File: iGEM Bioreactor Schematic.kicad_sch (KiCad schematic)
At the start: 13 parts, among them M1 Motor_AC, M2 Motor_Servo, Q1 Q_Photo_NPN, U1 OLED_display_1, U2 Pico, U3 L293D, U4 DS18B20, U5 L298N

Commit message: for datalogger
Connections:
- net at U2.1 (GPIO0/I2C0_SDA): now also U2.8 (GND)
- no-connect marks 44 -> 42
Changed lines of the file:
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@@
   (junction (at 172.72 74.93) (diameter 0) (color 0 0 0 0)
   )
-  (no_connect (at 93.98 44.45))
   (no_connect (at 124.46 171.45))
   (no_connect (at 121.92 171.45))
@@
   (no_connect (at 93.98 67.31))
   (no_connect (at 93.98 52.07))
-  (no_connect (at 93.98 62.23))
   (no_connect (at 93.98 64.77))
   (no_connect (at 144.78 82.55))
@@
     (stroke (width 0) (type default) (color 0 0 0 0))
   )
+  (wire (pts (xy 91.44 62.23) (xy 93.98 62.23))
+    (stroke (width 0) (type default) (color 0 0 0 0))
+  )
+  (wire (pts (xy 93.98 44.45) (xy 91.44 44.45))
+    (stroke (width 0) (type default) (color 0 0 0 0))
+  )
   (wire (pts (xy 147.32 46.99) (xy 151.13 46.99))
     (stroke (width 0) (type default) (color 0 0 0 0))
@@
     (stroke (width 0) (type default) (color 0 0 0 0))
   )
+  (wire (pts (xy 91.44 44.45) (xy 91.44 62.23))
+    (stroke (width 0) (type default) (color 0 0 0 0))
+  )

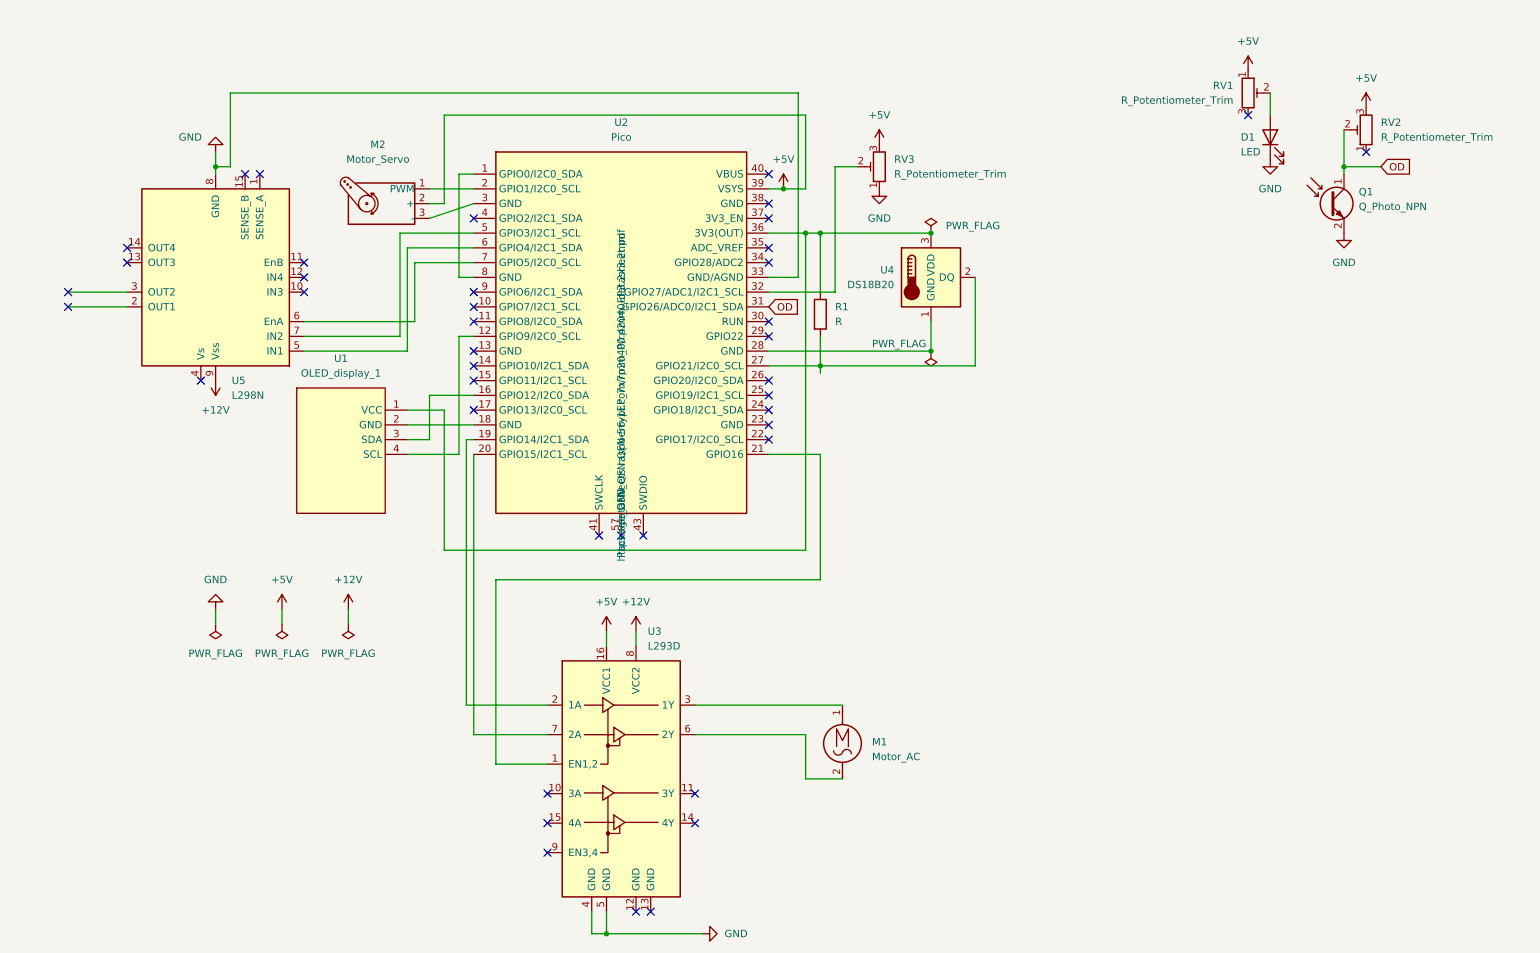
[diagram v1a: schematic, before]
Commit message: Clean up schematic
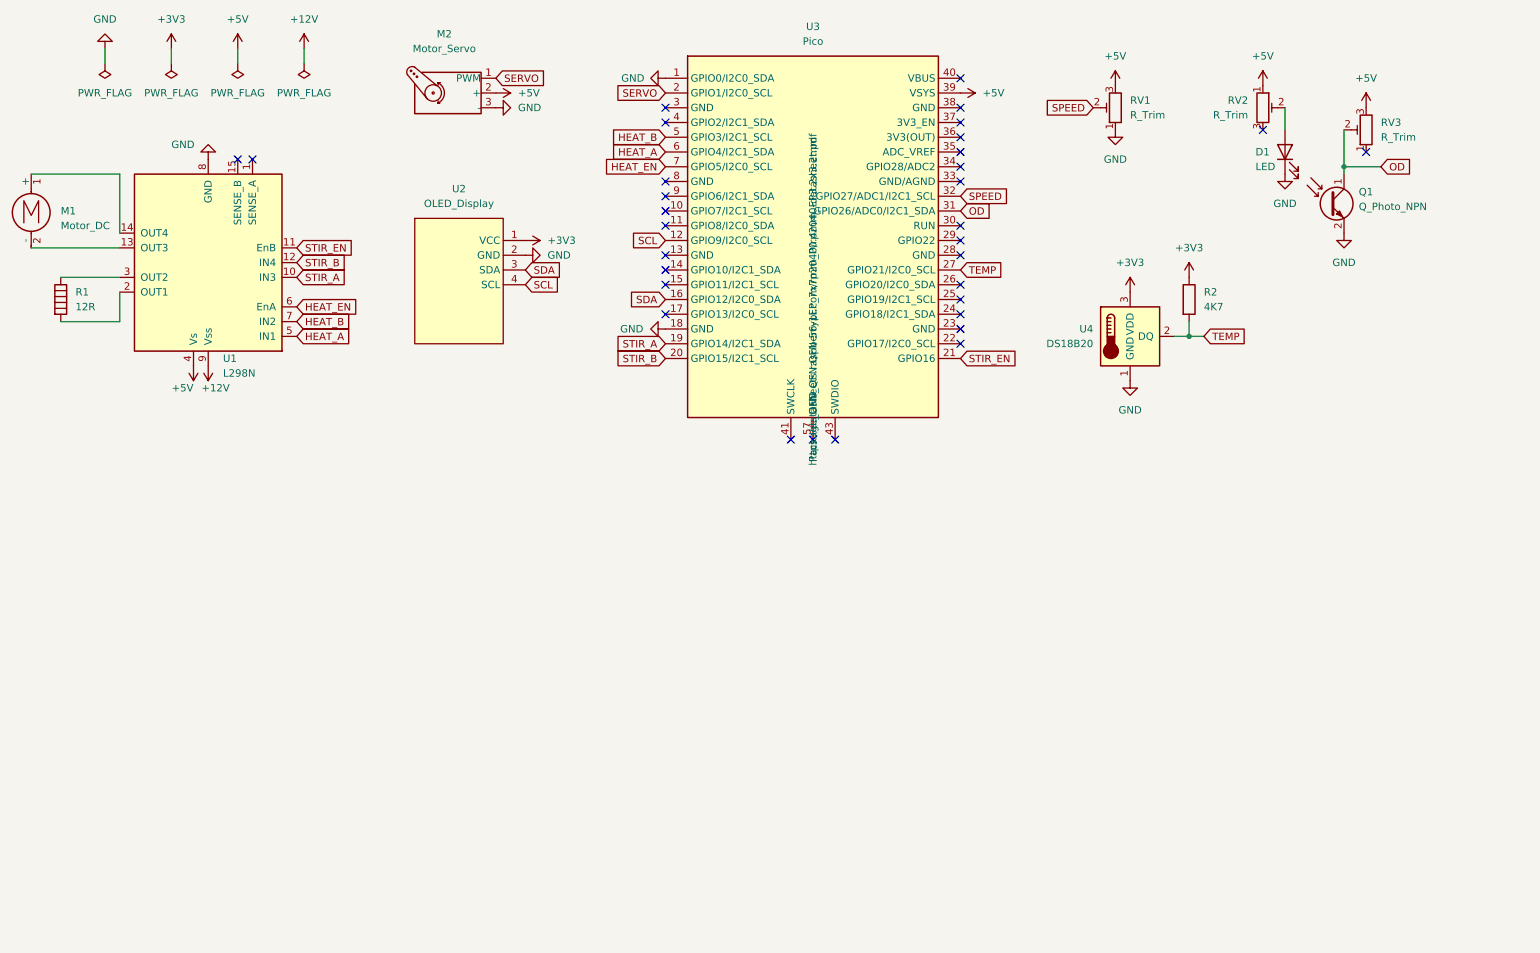
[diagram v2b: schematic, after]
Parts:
- removed M1: Motor_AC, symbol Motor:Motor_AC
- removed U3: L293D, Package_DIP:DIP-16_W7.62mm, symbol Driver_Motor:L293D
- added M1: Motor_DC, symbol Motor:Motor_DC
- added R1: 12R, symbol Device:Heater
- R2: renamed from R1; value R -> 4K7
- RV1: renamed from RV3; value R_Potentiometer_Trim -> R_Trim
- RV2: renamed from RV1; value R_Potentiometer_Trim -> R_Trim
- RV3: renamed from RV2; value R_Potentiometer_Trim -> R_Trim
- U2: renamed from U1; value OLED_display_1 -> OLED_Display
- renumbered U5 to U1, U2 to U3
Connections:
- net +5V: now also U1.4 (Vs)
- net GND: now also M2.3 (-), U2.2 (GND), U3.1 (GPIO0/I2C0_SDA), U3.18 (GND), U4.1 (GND); no longer U3.33 (GND/AGND)
- net STIR_EN: now reaches U3.21 (GPIO16)
- net STIR_EN: now also U1.11 (EnB)
- net STIR_A: now reaches U3.19 (GPIO14/I2C1_SDA)
- net STIR_A: now also U1.10 (IN3)
- net STIR_B: now reaches U3.20 (GPIO15/I2C1_SCL)
- net STIR_B: now also U1.12 (IN4)
- net SERVO: now reaches M2.1 (PWM), U3.2 (GPIO1/I2C0_SCL)
- net at U3.3 (GND): no longer M2.3 (-)
- net +3V3: now reaches R2.1, U2.1 (VCC), U4.3 (VDD)
- net +3V3: no longer U3.36 (3V3(OUT))
- net SDA: now reaches U2.3 (SDA), U3.16 (GPIO12/I2C0_SDA)
- net SCL: now reaches U2.4 (SCL), U3.12 (GPIO9/I2C0_SCL)
- net TEMP: now reaches R2.2, U3.27 (GPIO21/I2C0_SCL), U4.2 (DQ)
- net at U3.8 (GND): no longer U3.1 (GPIO0/I2C0_SDA)
- net at U3.28 (GND): no longer U4.1 (GND)
- net SPEED: now reaches RV1.2, U3.32 (GPIO27/ADC1/I2C1_SCL)
- net HEAT_B: now reaches U1.7 (IN2), U3.5 (GPIO3/I2C1_SCL)
- net HEAT_A: now reaches U1.5 (IN1), U3.6 (GPIO4/I2C1_SDA)
- net HEAT_EN: now reaches U1.6 (EnA), U3.7 (GPIO5/I2C0_SCL)
- net at U1.13 (OUT3): now also M1.2 (-)
- net at U1.14 (OUT4): now also M1.1 (+)
- net at U1.2 (OUT1): now also R1.2
- net at U1.3 (OUT2): now also R1.1
- no-connect marks 42 -> 32
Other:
- moved on the sheet: D1, R2, RV1, RV2, U1, U2, U3, U4

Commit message: Final grow experiments!
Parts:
- added RV?: R_Trim, symbol Device:R_Potentiometer_Trim
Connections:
- net +5V: now also RV?.3
- net GND: now also RV?.1
- net SET_OD: now reaches U3.34 (GPIO28/ADC2)
- net SET_OD: now also RV1.2
- net SPEED renamed SET_TEMP
- net SET_TEMP: now also RV?.2; no longer RV1.2
- no-connect marks 32 -> 31
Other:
- moved on the sheet: D1, Q1, R2, RV1, RV2, RV3, U4

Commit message: Add a reset button
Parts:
- added SW1: SW_Push, symbol Switch:SW_Push
- gave numbers to parts that had none: 1
- renumbered RV2 to RV1, RV3 to RV2, RV1 to RV3
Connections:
- net GND: now also SW1.2
- new net POWER: SW1.1
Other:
- moved on the sheet: RV3, RV4

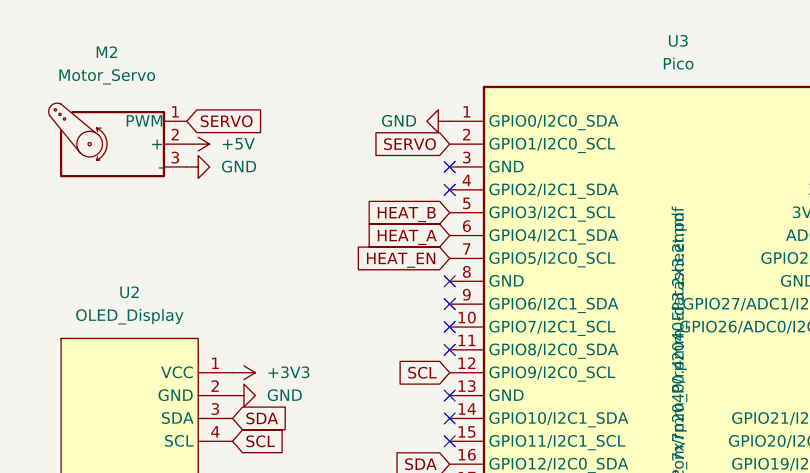
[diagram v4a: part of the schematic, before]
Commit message: Add the other end of the power flag
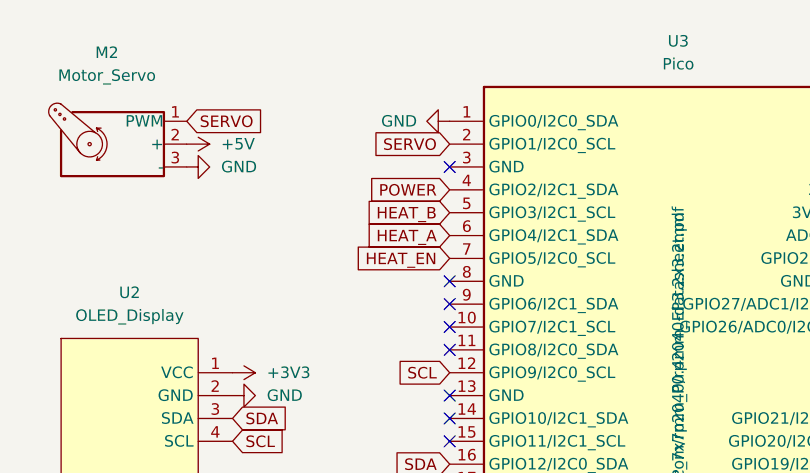
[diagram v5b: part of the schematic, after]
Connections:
- net POWER: now also U3.4 (GPIO2/I2C1_SDA)
- no-connect marks 31 -> 30
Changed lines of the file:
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@@
   (no_connect (at 127 53.34))
   (no_connect (at 127 50.8))
-  (no_connect (at 127 35.56))
   (no_connect (at 127 48.26))
   (no_connect (at 177.8 66.04))
@@
       (effects (font (size 1.27 1.27)) (justify right) hide)
     )
+  )
+  (global_label "POWER" (shape input) (at 127 35.56 180) (fields_autoplaced)
+    (effects (font (size 1.27 1.27)) (justify right))
+    (property "Intersheet References" "${INTERSHEET_REFS}" (id 0) (at 118.1159 35.4806 0)
+      (effects (font (size 1.27 1.27)) (justify right) hide)
+    )

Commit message: Final schematic?
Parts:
- removed RV3, RV4: R_Trim, symbol Device:R_Potentiometer_Trim
- added RV3, RV4: R_Pot, symbol Device:R_Potentiometer
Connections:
- net +5V: now also RV3.3, RV4.3
- net GND: now also U3.38 (GND), RV3.1, RV4.1; no longer U3.1 (GPIO0/I2C0_SDA), U3.18 (GND)
- net HEAT_B: now also U3.7 (GPIO5/I2C0_SCL); no longer U3.5 (GPIO3/I2C1_SCL)
- net HEAT_EN: now also U3.5 (GPIO3/I2C1_SCL); no longer U3.7 (GPIO5/I2C0_SCL)
- net SET_OD: now also RV3.2
- net SET_TEMP: now also RV4.2
- net PUMP_EN: now reaches U3.17 (GPIO13/I2C0_SCL)
- net PUMP_EN: now also U1.11 (EnB)
- net STIR_A renamed PUMP_A
- net STIR_B renamed PUMP_B
- net STIR_EN: no longer names the net of U3.21 (GPIO16)
- net STIR_EN: no longer U1.11 (EnB)
- no-connect marks 30 -> 31
